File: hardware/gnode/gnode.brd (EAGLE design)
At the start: 50 x 25 mm, 27 parts, among them U1 ATMEGA328P_TQFP, U3 MCP1700TT, U4 CN3083, U5 HTU21D

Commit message: OCD improvements
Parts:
- moved R2 2.50 mm to (12.4, 18.0), turned to 270 degrees
- moved C2 1.05 mm to (10.4, 18.0), turned to 270 degrees
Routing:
- net GND: track 9.18 -> 12.0 mm, vias 38 -> 41
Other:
- board text added: "1"
- board text added: "2"
- board text added: "TEST"
- board text removed: "TP"

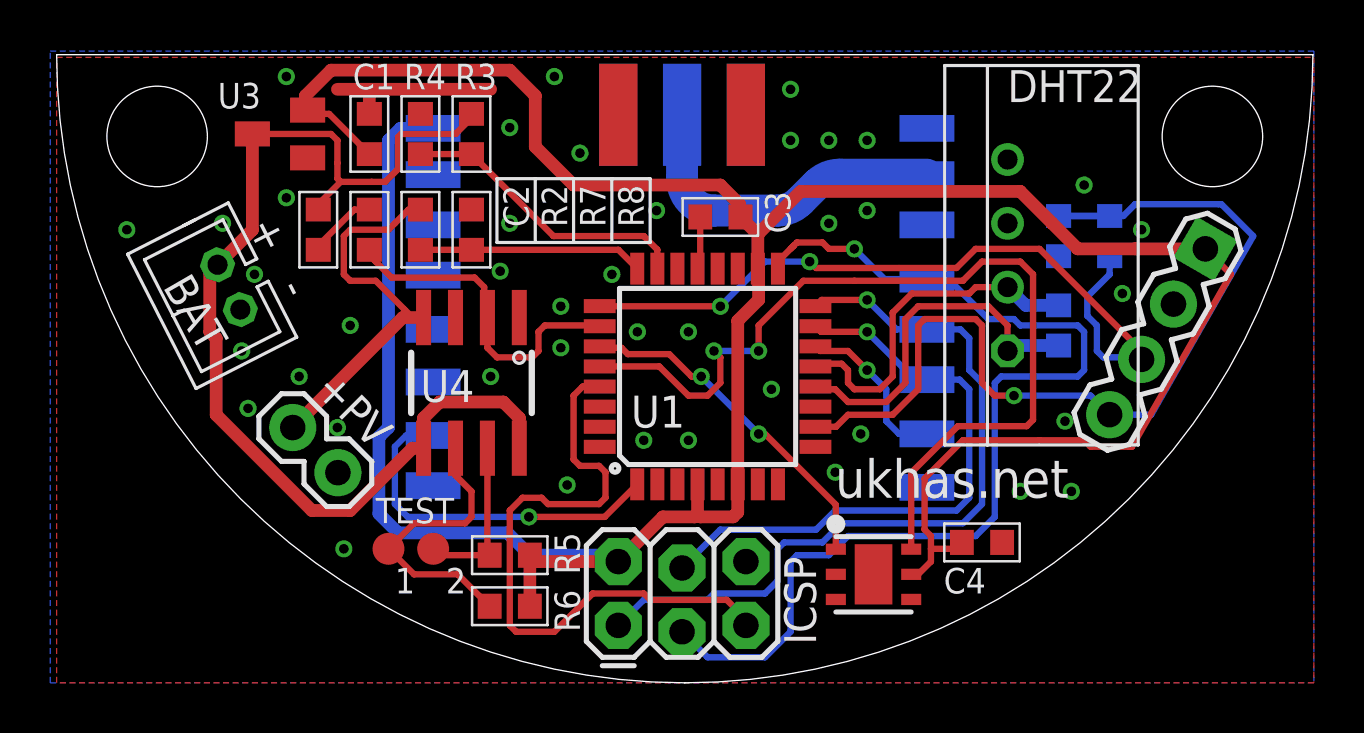
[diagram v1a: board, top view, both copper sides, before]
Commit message: uart broken out
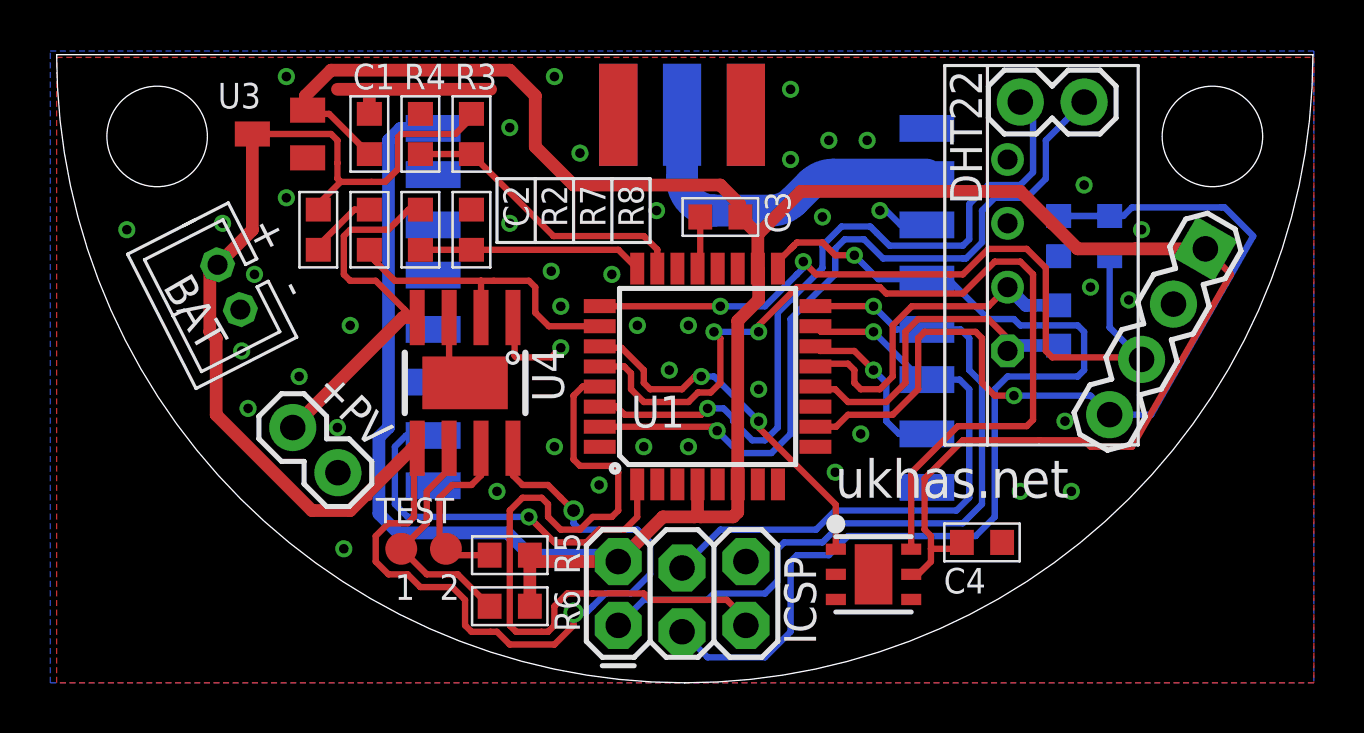
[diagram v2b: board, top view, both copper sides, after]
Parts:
- added JP4: (no value), Mine:1X02
- U4: device jonsowman:SOIC8 -> jonsowman:SO8-PAD
- moved TP1 0.51 mm to (15.5, 5.33)
- moved TP2 0.51 mm to (13.7, 5.33)
- moved U4 0.25 mm to (16.3, 11.9)
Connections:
- new net RX: JP4.1, U1.30
- new net TX: JP4.2, U1.31
- net GND: now also U4.PAD
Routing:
- net TX: track 0.00 -> 31.0 mm, vias 0 -> 1
- net RX: track 0.00 -> 30.2 mm, vias 0 -> 1
- net VBATT: track 43.4 -> 65.8 mm, vias 0 -> 2
- net GND: track 12.0 -> 20.3 mm, vias 41 -> 44
- net NRST: track 26.0 -> 28.9 mm
- net N$5: track 11.8 -> 9.26 mm
- net RFM_DIO0: track 14.4 -> 16.0 mm
- net GPIO0: track 38.2 -> 37.1 mm
- net DHT22_VCC: track 14.4 -> 13.4 mm
- net SHT_DATA: track 13.8 -> 14.6 mm
- net SHT_SCK: track 36.4 -> 37.2 mm
- net ISET: track 13.4 -> 12.6 mm
- net N$2: track 6.65 -> 7.21 mm
- net GPIO1: track 31.0 -> 31.5 mm
- net VPANEL: track 15.9 -> 15.4 mm
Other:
- board text added: "+"
- board text added: "-"
- board text added: "RX"
- board text added: "TX"
- board text removed: "GND"
- board text removed: "VCC"

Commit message: bottom pad and heatsinking for cn3083
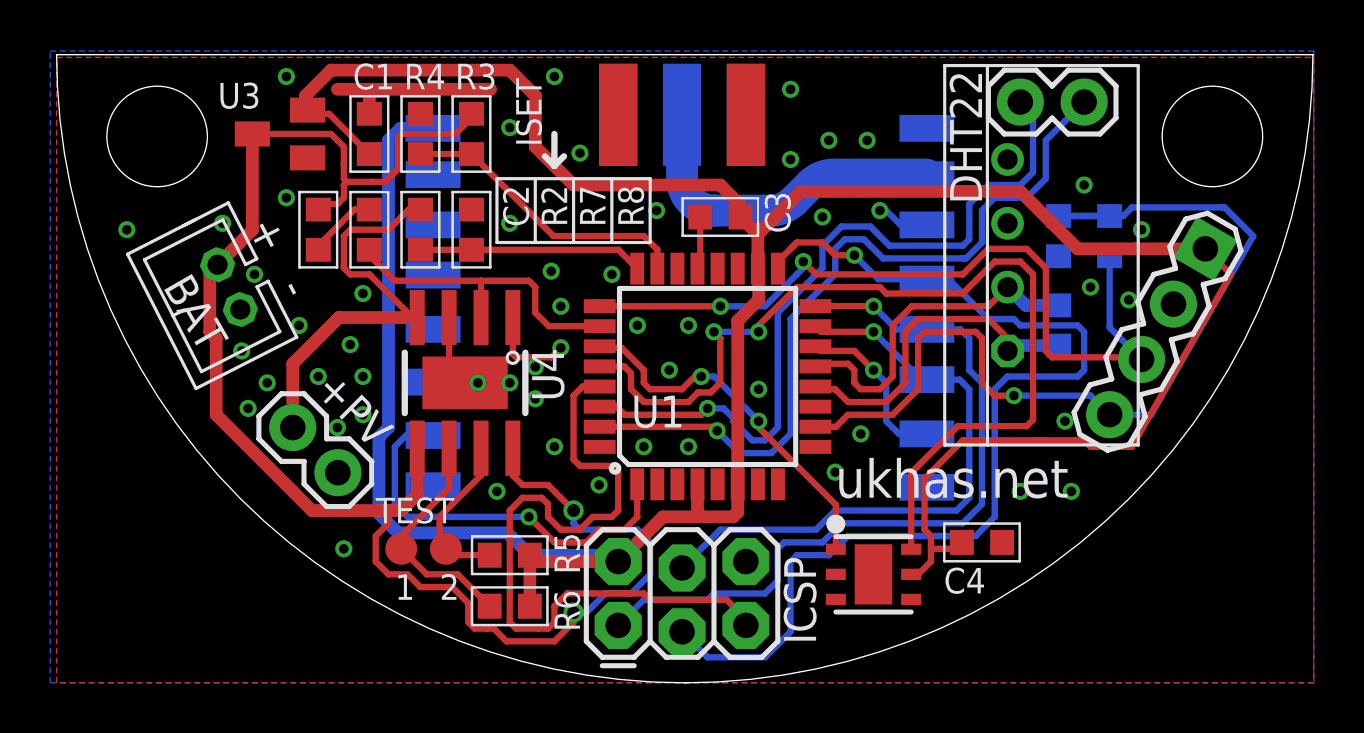
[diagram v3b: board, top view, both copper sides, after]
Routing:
- net VBATT: track 65.8 -> 63.4 mm
- net VPANEL: track 15.4 -> 16.7 mm
- net GND: vias 44 -> 53
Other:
- board text added: "ISET"

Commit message: added caps for cn3083, oops
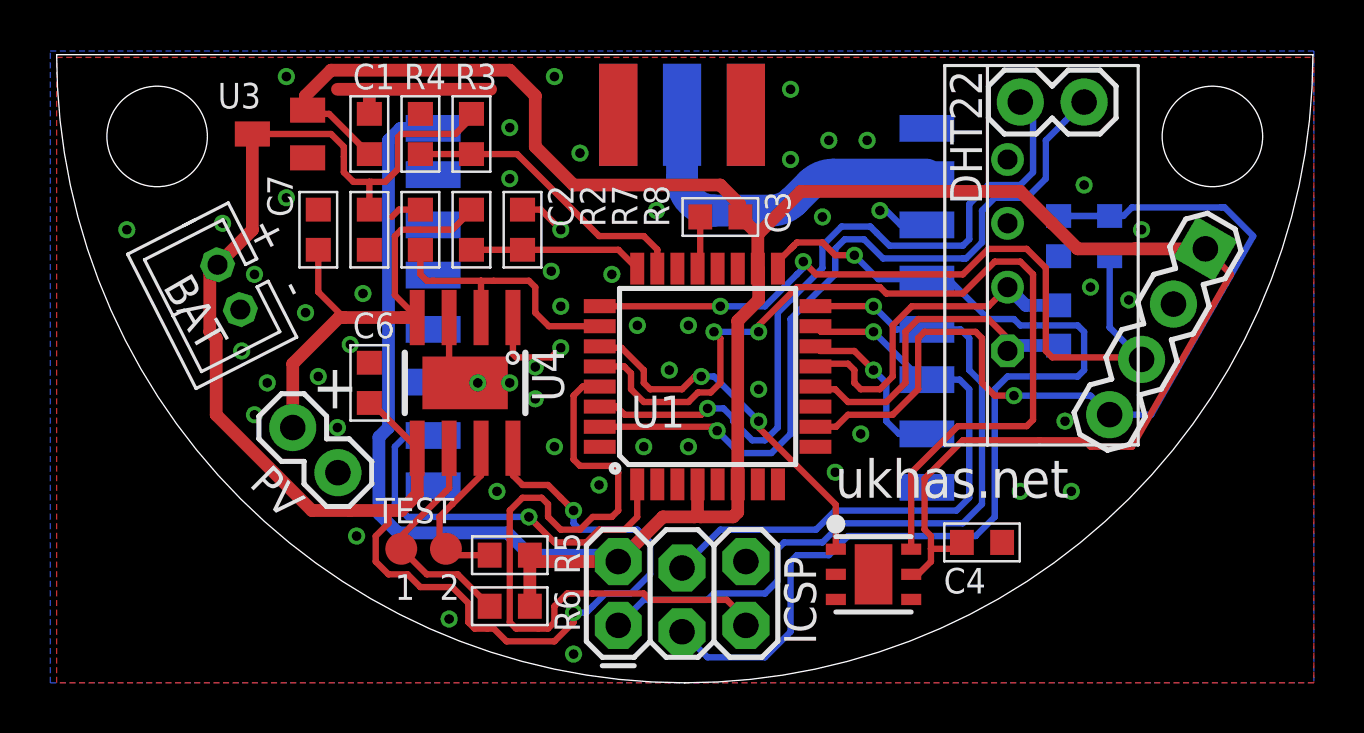
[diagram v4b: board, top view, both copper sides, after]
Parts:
- added C6: 4u7, passives-7351:C0603-N
- added C7: 22u, passives-7351:C0603-N
- moved R7 2.03 mm to (16.5, 18.0)
- moved C2 2.03 mm to (12.4, 18.0)
- moved R2 2.03 mm to (14.5, 18.0)
- moved R8 2.03 mm to (18.5, 18.0)
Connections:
- net GND: now also C6.2, C7.2
- net VBATT: now also C6.1
- net VPANEL: now also C7.1
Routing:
- net VSENSE_PANEL: track 8.94 -> 6.91 mm
- net VPANEL: track 16.7 -> 18.7 mm
- net ISET: track 12.6 -> 11.0 mm
- net VBATT: track 63.4 -> 65.0 mm
- net GND: track 20.3 -> 20.6 mm, vias 53 -> 54
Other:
- board text added: "PV"
- board text removed: "+PV"
- board text removed: "ISET"
